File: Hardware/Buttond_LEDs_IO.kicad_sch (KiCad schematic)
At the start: 9 parts, among them J13 SFH11-PBPC-D05-ST-BK

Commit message: revB updates
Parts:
- added C18: 0.1u, Capacitor_SMD:C_0603_1608Metric, symbol Device:C
- added R22, R23: 10k, Resistor_SMD:R_0603_1608Metric, symbol Device:R_US
- added SW1: RESET, UTSVT_Special:SW_SPST_B3SL-1002P, symbol Switch:SW_MEC_5G
- added SW2: BOOT, UTSVT_Special:SW_CJS-1200TA, symbol Switch:SW_SPDT
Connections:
- net GND: now also C18.2, SW1.1 (A), SW1.2 (A), SW2.3 (C)
- new net: R23.1, SW2.2 (B)
- new net +3.3V_ESP: R22.1, SW2.1 (A)
- new net BOOT: R23.2
- new net Reset: C18.1, R22.2, SW1.3 (B), SW1.4 (B)

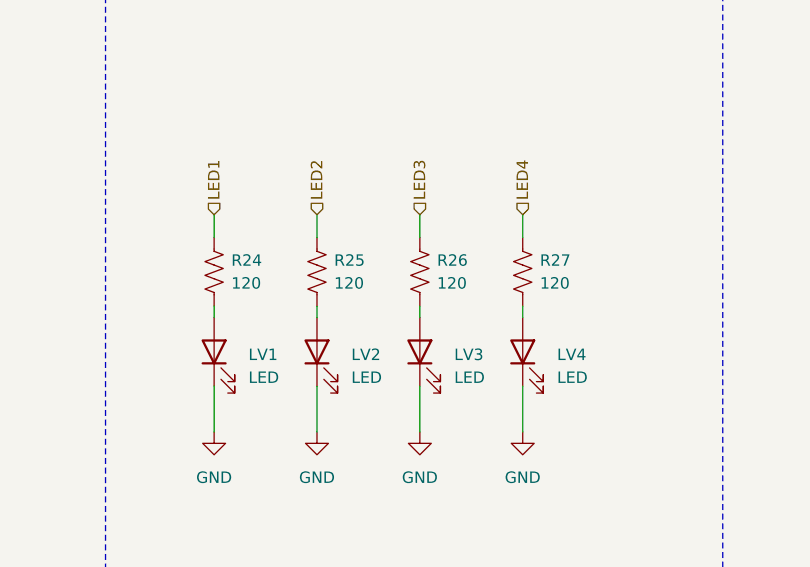
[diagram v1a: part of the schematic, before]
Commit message: Schematic polishes, layout WIP
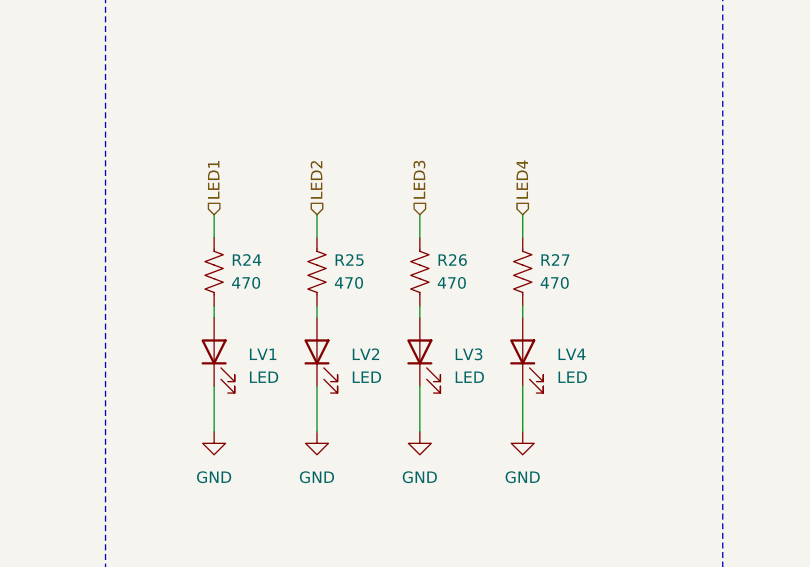
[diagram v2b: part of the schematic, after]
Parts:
- R24, R25, R26, R27: value 120 -> 470
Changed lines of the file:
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@@
 			)
 		)
-		(property "Value" "120"
+		(property "Value" "470"
 			(at 123.19 93.9799 0)
 			(effects
@@
 			)
 		)
-		(property "Value" "120"
+		(property "Value" "470"
 			(at 134.62 93.9799 0)
 			(effects
@@
 			)
 		)
-		(property "Value" "120"
+		(property "Value" "470"
 			(at 146.05 93.9799 0)
 			(effects
@@
 			)
 		)
-		(property "Value" "120"
+		(property "Value" "470"
 			(at 157.48 93.9799 0)
 			(effects

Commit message: circuit blocks designed, schematic updated
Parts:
- removed J13: SFH11-PBPC-D05-ST-BK, UTSVT_Connectors:CONN_SFH11-xxxC-D05-ST-XX_SUL, symbol UTSVT_Connectors:SFH11-PBPC-D05-ST-BK

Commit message: intial layout design
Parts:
- SW1: footprint UTSVT_Special:SW_SPST_B3SL-1002P -> TL3365AF180QG:TL3365AF180QG
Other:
- note removed: "ESP Broken Out IO"
- moved on the sheet: C18, LV1, LV2, LV3, LV4, R22, R23, R24, R25, R26, R27, SW1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

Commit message: JLC Production Files
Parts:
- C18: LCSC (none) -> C14663
- LV1, LV2, LV3, LV4: LCSC (none) -> C7371904
- R22, R23: LCSC (none) -> C25804
- R24, R25, R26, R27: LCSC (none) -> C23179
- SW1: LCSC (none) -> C2886926
- SW2: LCSC (none) -> C2921628
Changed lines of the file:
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@@
+			)
+		)
+		(property "LCSC" "C2921628"
+			(at 119.761 131.318 0)
+			(effects
+				(font
+					(size 1.27 1.27)
+				)
+				(hide yes)
 			)
 		)
@@
 			)
 		)
+		(property "LCSC" "C7371904"
+			(at 184.15 106.9974 0)
+			(effects
+				(font
+					(size 1.27 1.27)
+				)
+				(hide yes)
+			)
+		)
 		(pin "1"
 		)
@@
 			)
 		)
+		(property "LCSC" "C23179"
+			(at 182.245 96.5199 0)
+			(effects
+				(font
+					(size 1.27 1.27)
+				)
+				(hide yes)
+			)
+		)
 		(pin "1"
 		)
@@
 			)
 		)
+		(property "LCSC" "C14663"
+			(at 99.441 74.676 0)
+			(effects
+				(font
+					(size 1.27 1.27)
+				)
+				(hide yes)
+			)
+		)
 		(pin "1"
 		)
@@
 			)
 		)
+		(property "LCSC" "C25804"
+			(at 100.965 63.4999 0)
+			(effects
+				(font
+					(size 1.27 1.27)
+				)
+				(hide yes)
+			)
+		)
 		(pin "1"
 		)
@@
 			)
 		)
+		(property "LCSC" "C23179"
+			(at 193.675 96.5199 0)
+			(effects
+				(font
+					(size 1.27 1.27)
+				)
+				(hide yes)
+			)
+		)
 		(pin "1"
 		)
@@
 			)
 		)
+		(property "LCSC" "C7371904"
+			(at 195.58 106.9974 0)
+			(effects
+				(font
+					(size 1.27 1.27)
+				)
+				(hide yes)
+			)
+		)
 		(pin "1"
 		)
@@
 			)
 		)
+		(property "LCSC" "C23179"
+			(at 205.105 96.5199 0)
+			(effects
+				(font
+					(size 1.27 1.27)
+				)
+				(hide yes)
+			)
+		)
 		(pin "1"
 		)
@@
 			)
 		)
+		(property "LCSC" "C23179"
+			(at 216.535 96.5199 0)
+			(effects
+				(font
+					(size 1.27 1.27)
+				)
+				(hide yes)
+			)
+		)
 		(pin "1"
 		)
@@
 			)
 		)
+		(property "LCSC" "C2886926"
+			(at 113.665 62.23 0)
+			(effects
+				(font
+					(size 1.27 1.27)
+				)
+				(hide yes)
+			)
+		)
 		(pin "2"
 		)
@@
 			)
 		)
+		(property "LCSC" "C7371904"
+			(at 218.44 106.9974 0)
+			(effects
+				(font
+					(size 1.27 1.27)
+				)
+				(hide yes)
+			)
+		)
 		(pin "1"
 		)
@@
 			)
 		)
+		(property "LCSC" "C7371904"
+			(at 207.01 106.9974 0)
+			(effects
+				(font
+					(size 1.27 1.27)
+				)
+				(hide yes)
+			)
+		)
 		(pin "1"
 		)
@@
 			(effects
 				(font
+					(size 1.27 1.27)
+				)
+				(hide yes)
+			)
+		)
+		(property "LCSC" "C25804"
+			(at 109.22 119.38 0)
+			(effects
+				(font

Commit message: condensed custom lirbraries
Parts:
- SW1: footprint TL3365AF180QG:TL3365AF180QG -> CustomKiCad-Library:TL3365AF180QG
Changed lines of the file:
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@@
 			)
 		)
-		(property "Footprint" "TL3365AF180QG:TL3365AF180QG"
+		(property "Footprint" "CustomKiCad-Library:TL3365AF180QG"
 			(at 113.665 64.77 0)
 			(effects

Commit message: JLCPCB ouput files
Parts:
- R24, R25, R26, R27: P/N CRCW0603120RFKEC -> CRCW1206470RFKEA
